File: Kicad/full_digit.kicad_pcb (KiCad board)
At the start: 2 copper layers, 106.7 x 152.4 mm, 48 parts, among them J1 CONN_8, J2 CONN_8, J3 CONN_8, J4 CONN_8, J5 CONN_8, J6 CONN_8, J7 CONN_8, J8 CONN_8, T0 TP, T1 TP, T2 TP, T3 TP, T4 TP, T5 TP, T6 TP, T7 TP, U1 TLC5917, X1 MTHOLE, X2 MTHOLE, X3 MTHOLE, X4 MTHOLE

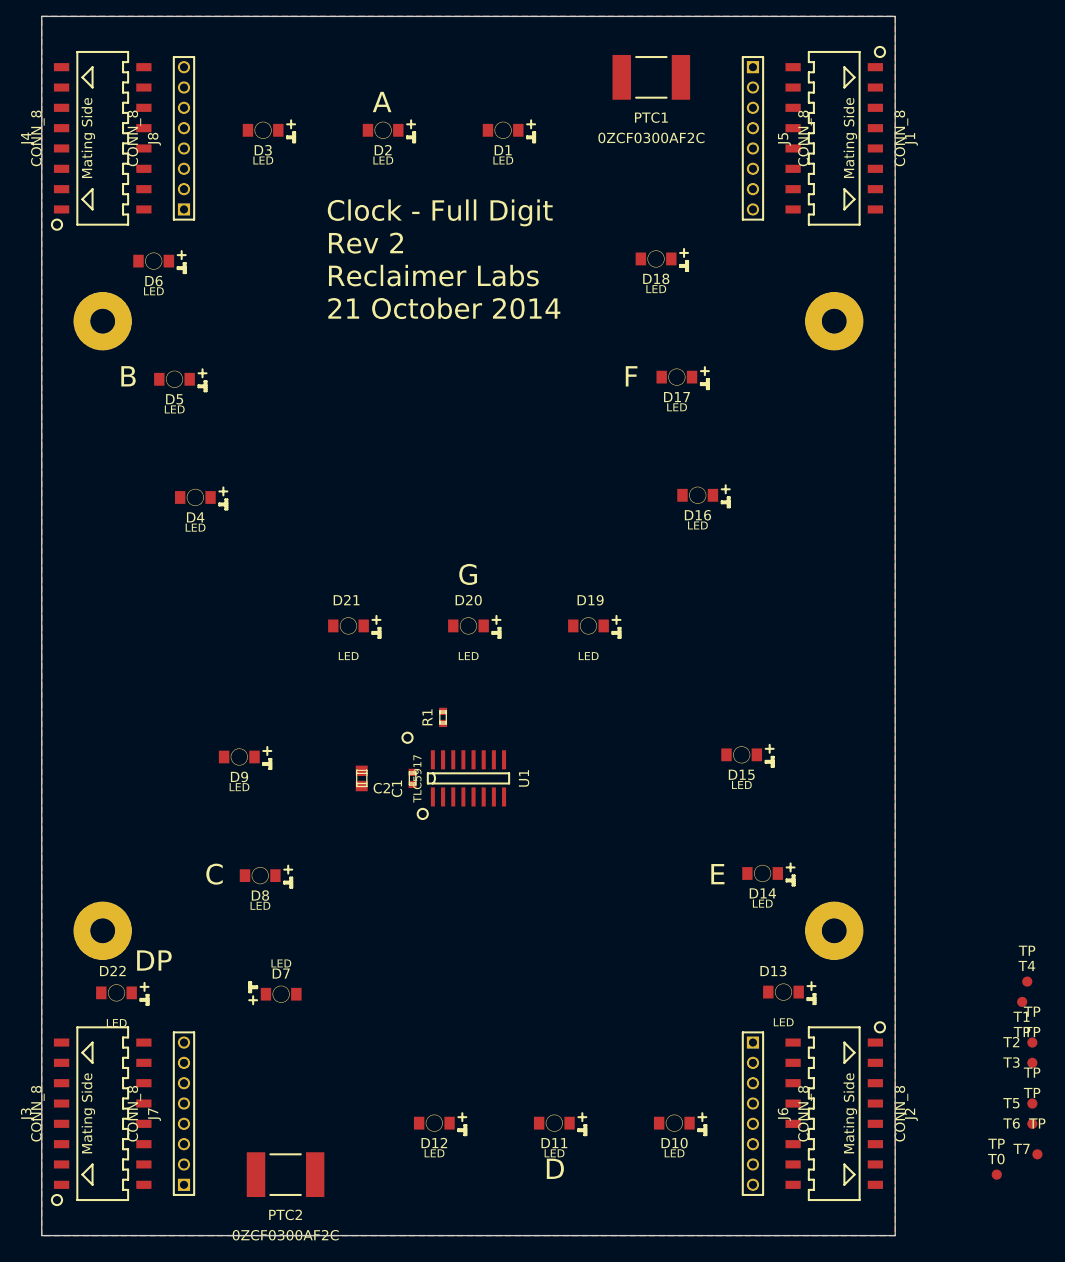
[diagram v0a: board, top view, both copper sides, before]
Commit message: Mechanical and Logo Updates
Updated Reclaimer Labs Logo as per issue #11. Also added thru-hole
connectors to layout as per issue #9. Mounting holes have been moved as
per issue #8. LED hole is replaced with slot as per issue #7, might need
to be tweaked to reduce rotation during assembly. Inter-board connector
silkscreen is updated to more easily show mating side vs non-mating side
as per issue #5. Initial commit of gerbers.
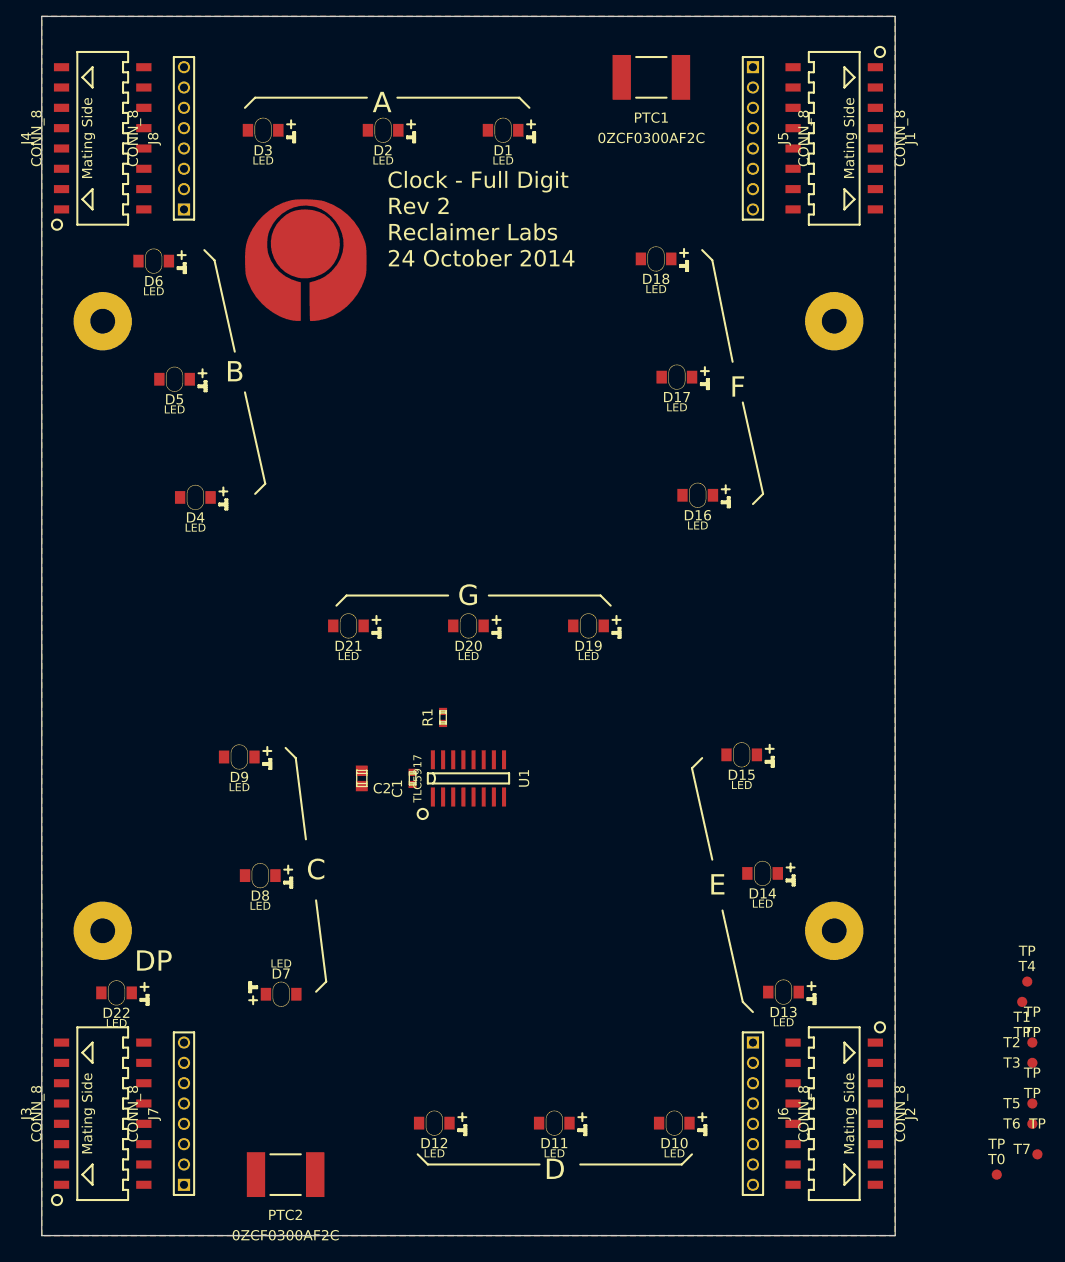
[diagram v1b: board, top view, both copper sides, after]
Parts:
- added G***: LOGO, LOGO, F.Cu at (101.6, 99.1)
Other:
- board text added: "Clock - Full Digit Rev 2 Reclaimer Labs 24 October 2014"
- board text removed: "Clock - Full Digit Rev 2 Reclaimer Labs 21 October 2014"

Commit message: Added pin labels
Added labels on all input and output pins as per issue #5.
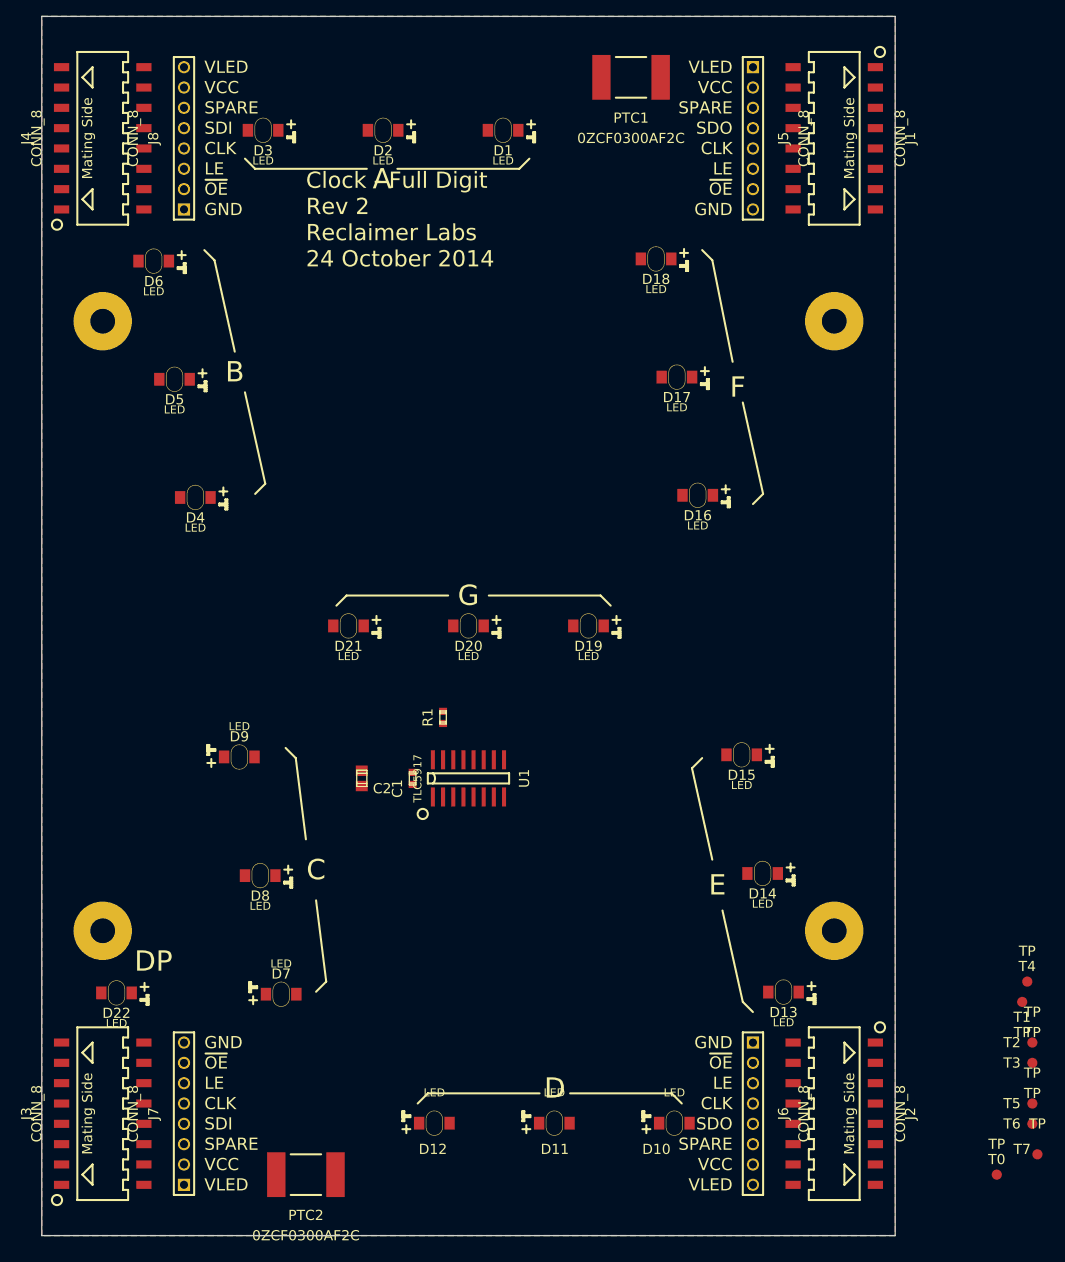
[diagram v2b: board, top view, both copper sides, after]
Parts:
- removed G***: LOGO, LOGO
- moved PTC1 2.54 mm to (142.2, 76.2)
- moved PTC2 2.54 mm to (101.6, 213.4)
- turned D10 to 0 degrees
- turned D11 to 0 degrees
- turned D12 to 0 degrees
- turned D9 to 0 degrees
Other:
- board text added: "CLK"
- board text added: "GND"
- board text added: "LE"
- board text added: "SDI"
- board text added: "SDO"
- board text added: "SPARE"
- board text added: "VCC"
- board text added: "VLED"
- board text added: "~OE"

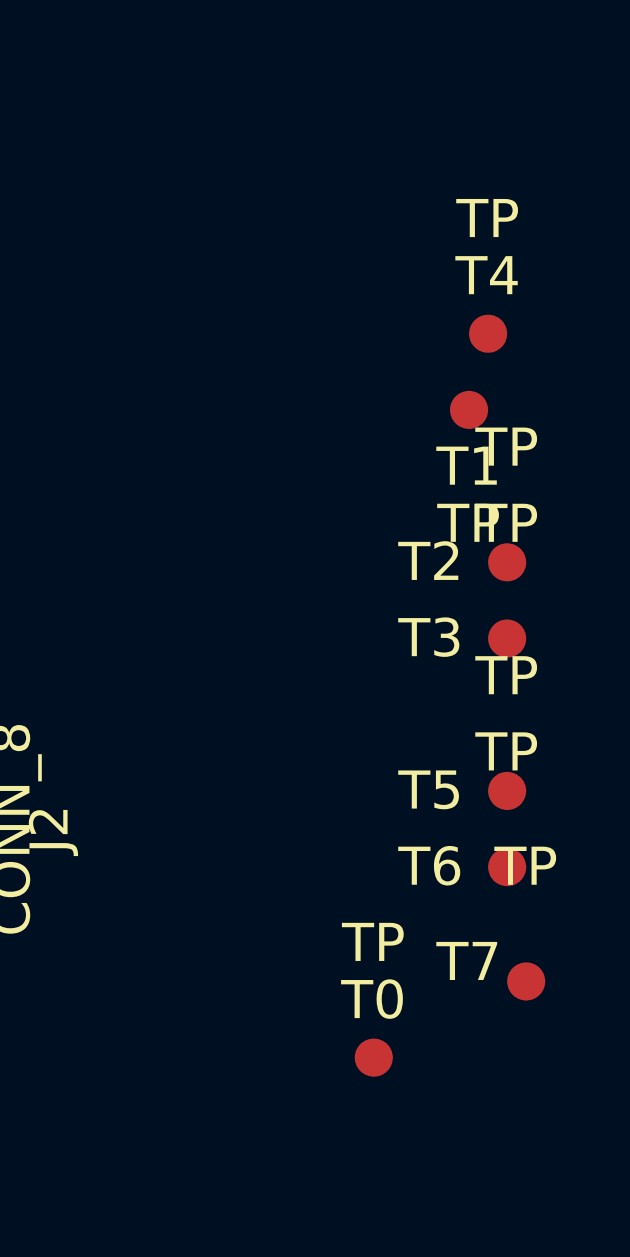
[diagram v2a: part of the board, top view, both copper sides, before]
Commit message: Removed test points
Removed test points T0-T7. They are unnecessary, as the pins on U1 and
the LEDs provide a good enough interface. If they are needed for
pogo-pin type testing, they can be added back in.
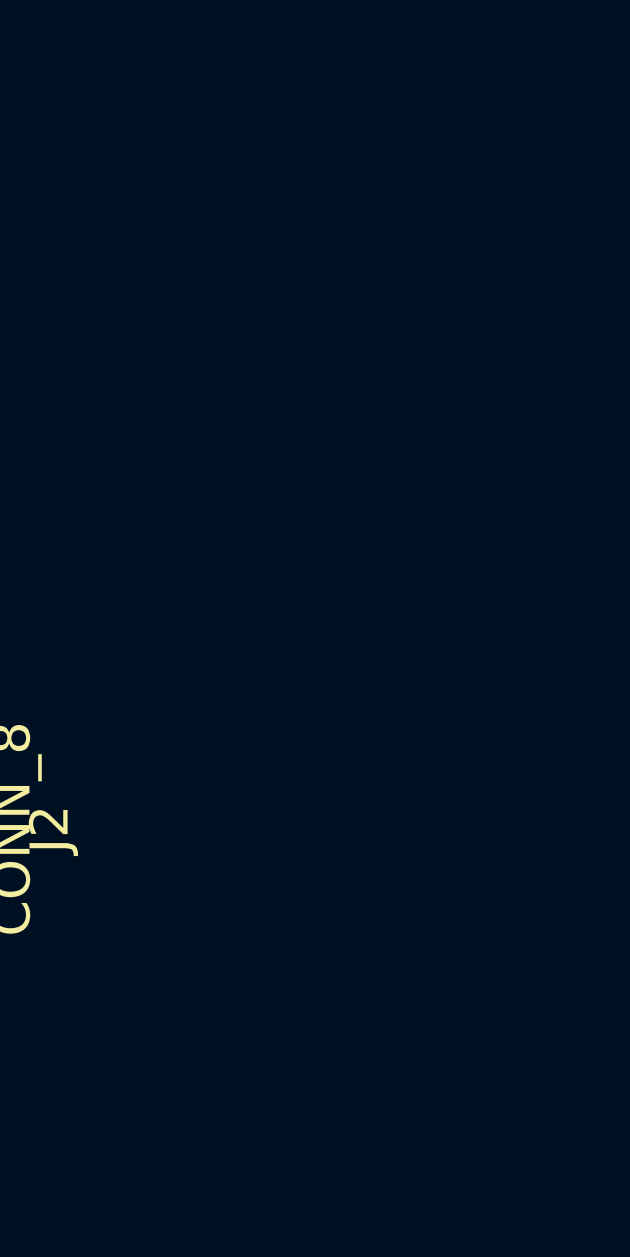
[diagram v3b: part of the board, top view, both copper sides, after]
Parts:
- removed T0, T1, T2, T3, T4, T5, T6, T7: TP, TP

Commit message: Rev 2 Feature Complete
Possible final draft of Rev 2 layout.
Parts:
- moved D10 30.0 mm to (117.7, 206.9)
- moved D12 30.0 mm to (147.7, 206.9)
- moved C2 24.8 mm to (92.7, 144.8), turned to 180 degrees
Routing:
- net Vled: track 0.00 -> 510.2 mm, vias 0 -> 10
- net VCC: track 0.00 -> 385.4 mm, vias 0 -> 2
- net /CLK: track 0.00 -> 355.0 mm, vias 0 -> 2
- net /LE: track 0.00 -> 347.7 mm, vias 0 -> 2
- net /SPARE: track 0.00 -> 340.9 mm, vias 0 -> 1
- net /~OE: track 0.00 -> 334.8 mm, vias 0 -> 2
- net /SDI: track 0.00 -> 286.7 mm, vias 0 -> 3
- net GND: track 0.00 -> 249.6 mm, vias 0 -> 36
- net /SDO: track 0.00 -> 207.6 mm, vias 0 -> 2
- net N-0000010: track 0.00 -> 132.0 mm, vias 0 -> 2
- net N-000006: track 0.00 -> 123.8 mm, vias 0 -> 2
- net N-000003: track 0.00 -> 90.6 mm, vias 0 -> 2
- net N-000005: track 0.00 -> 75.7 mm, vias 0 -> 2
- net N-000009: track 0.00 -> 54.7 mm
- net N-000008: track 0.00 -> 52.8 mm, vias 0 -> 2
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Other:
- net class SuperWide added: clearance 0.1524, trace_width 2.54, via_dia 1.143, via_drill 0.635
- board text added: "Seven Segment Display Rev 2 Reclaimer Labs 25 October 2014"
- board text removed: "Clock - Full Digit Rev 2 Reclaimer Labs 24 October 2014"

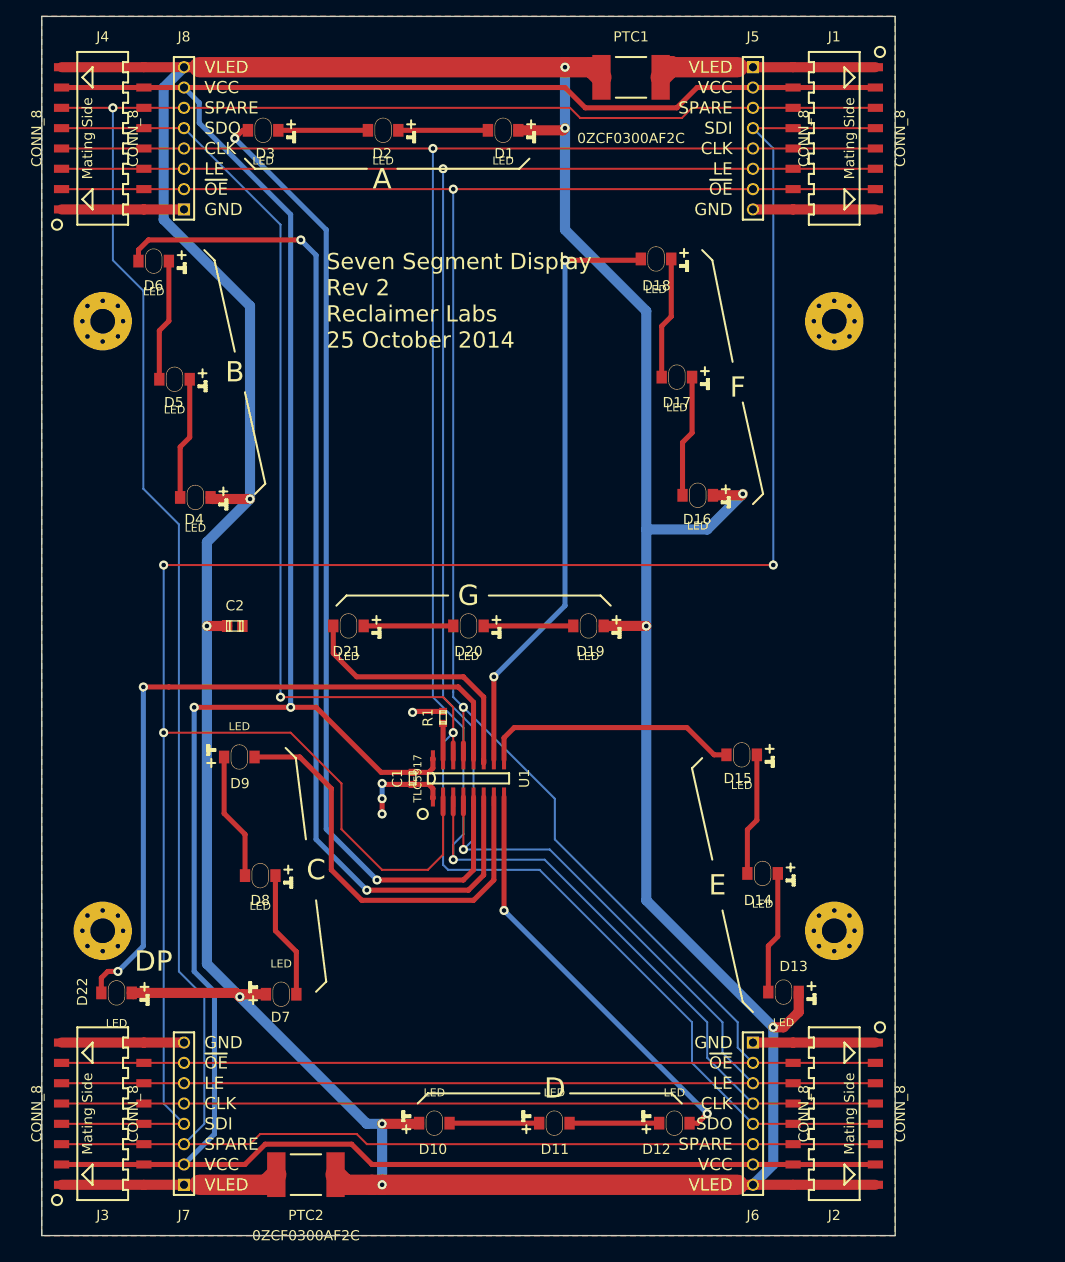
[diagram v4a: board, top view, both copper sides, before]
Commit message: Layout Tweaks
Updated silkscreen to include voltage ranges. Updated tracks into all
parts to balance and center tracks in and out.
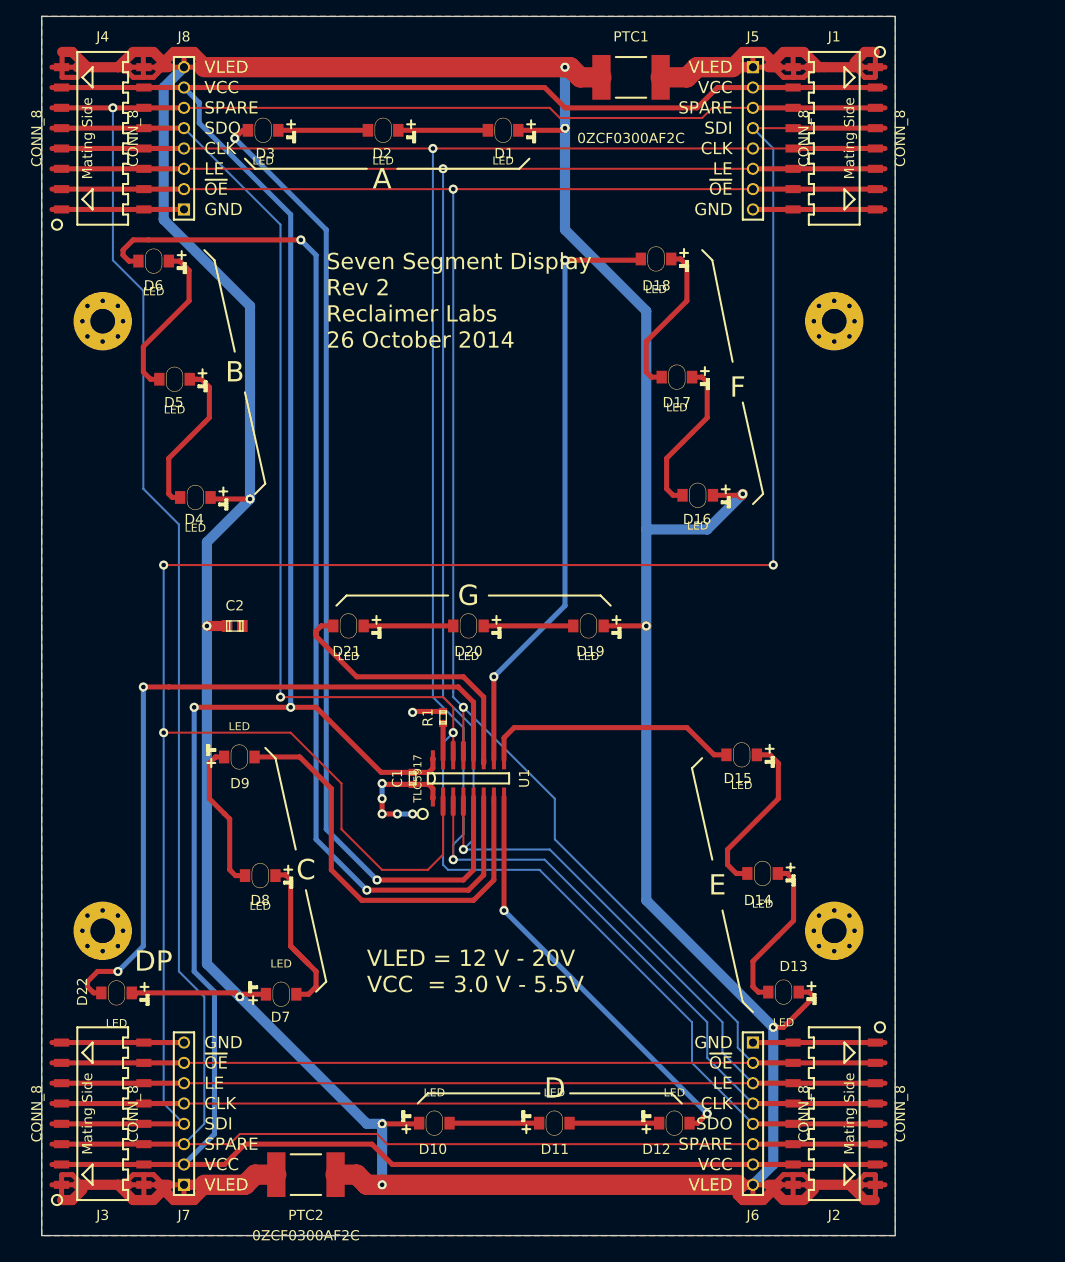
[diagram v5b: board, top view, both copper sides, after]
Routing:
- net Vled: track 510.2 -> 588.7 mm
- net N-0000034: track 29.2 -> 65.0 mm
- net N-0000020: track 28.9 -> 64.6 mm
- net GND: track 249.6 -> 258.2 mm, vias 36 -> 38
- net N-0000023: track 15.9 -> 22.9 mm
- net N-0000015: track 15.3 -> 21.4 mm
- net N-0000029: track 15.3 -> 20.8 mm
- net N-0000028: track 15.3 -> 20.4 mm
- net VCC: track 385.4 -> 390.2 mm
- net /~OE: track 334.8 -> 339.6 mm
- net /SPARE: track 340.9 -> 345.7 mm
- net /LE: track 347.7 -> 352.6 mm
- net /CLK: track 355.0 -> 359.8 mm
- net N-0000011: track 15.3 -> 19.9 mm
- net N-0000014: track 15.3 -> 19.9 mm
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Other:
- board text added: "Seven Segment Display Rev 2 Reclaimer Labs 26 October 2014"
- board text added: "VLED = 12 V - 20V VCC = 3.0 V - 5.5V"
- board text removed: "Seven Segment Display Rev 2 Reclaimer Labs 25 October 2014"
